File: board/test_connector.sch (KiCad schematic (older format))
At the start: 1 part, among them P1 test_connector

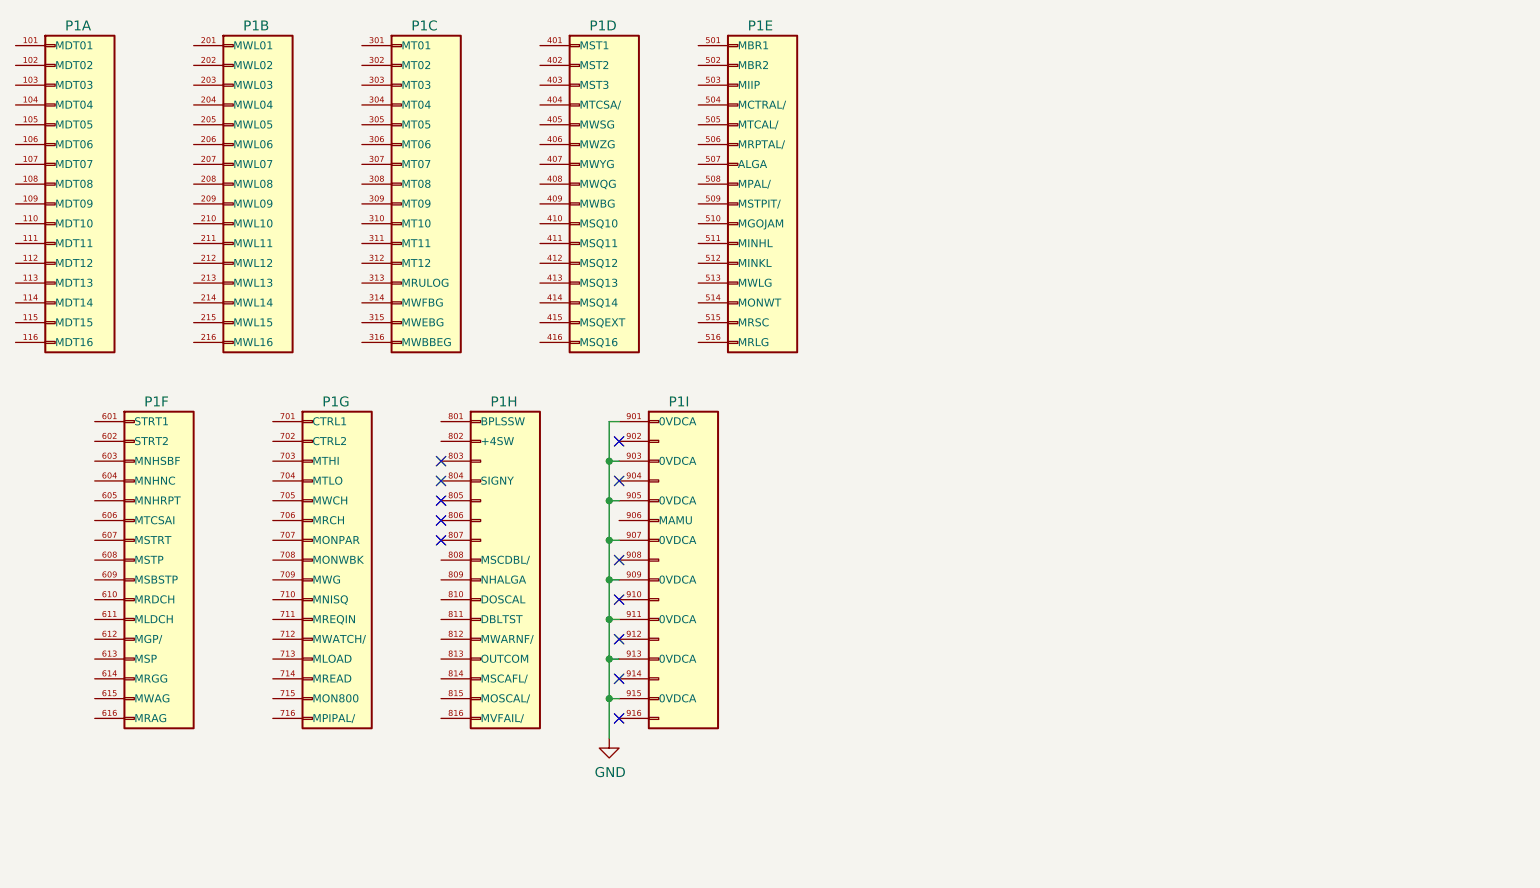
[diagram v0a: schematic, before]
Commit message: Board: initial schematic for the monitor interface board
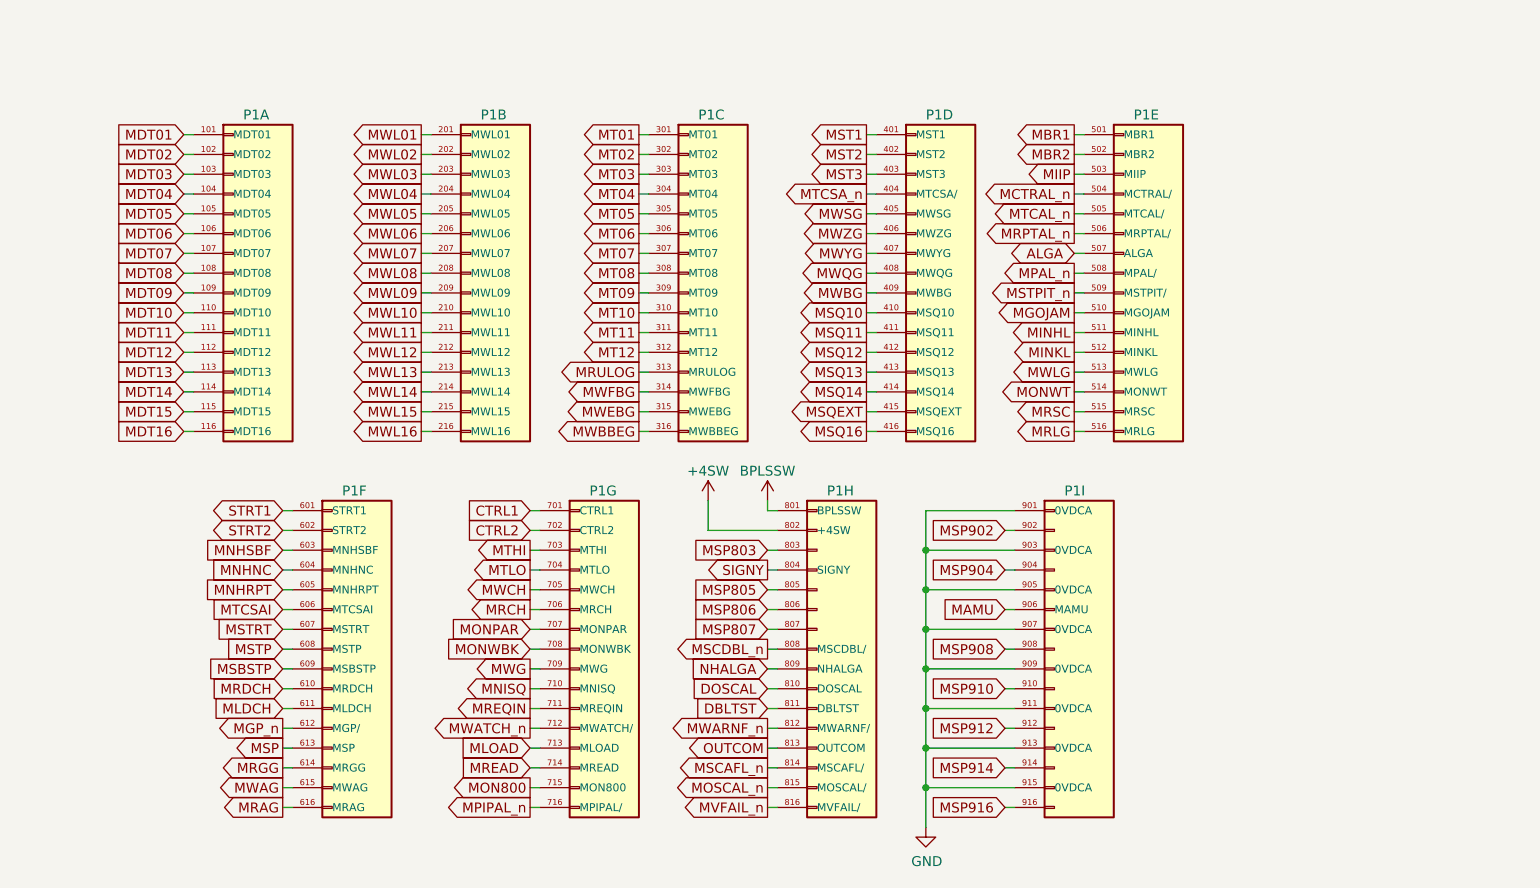
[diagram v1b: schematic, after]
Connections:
- net MDT01: now reaches P1.101 (MDT01)
- net MDT02: now reaches P1.102 (MDT02)
- net MDT03: now reaches P1.103 (MDT03)
- net MDT04: now reaches P1.104 (MDT04)
- net MDT05: now reaches P1.105 (MDT05)
- net MDT06: now reaches P1.106 (MDT06)
- net MDT07: now reaches P1.107 (MDT07)
- net MDT08: now reaches P1.108 (MDT08)
- net MDT09: now reaches P1.109 (MDT09)
- net MDT10: now reaches P1.110 (MDT10)
- net MDT11: now reaches P1.111 (MDT11)
- net MDT12: now reaches P1.112 (MDT12)
- net MDT13: now reaches P1.113 (MDT13)
- net MDT14: now reaches P1.114 (MDT14)
- net MDT15: now reaches P1.115 (MDT15)
- net MDT16: now reaches P1.116 (MDT16)
- net MWL01: now reaches P1.201 (MWL01)
- net MWL02: now reaches P1.202 (MWL02)
- net MWL03: now reaches P1.203 (MWL03)
- net MWL04: now reaches P1.204 (MWL04)
- net MWL05: now reaches P1.205 (MWL05)
- net MWL06: now reaches P1.206 (MWL06)
- net MWL07: now reaches P1.207 (MWL07)
- net MWL08: now reaches P1.208 (MWL08)
- net MWL09: now reaches P1.209 (MWL09)
- net MWL10: now reaches P1.210 (MWL10)
- net MWL11: now reaches P1.211 (MWL11)
- net MWL12: now reaches P1.212 (MWL12)
- net MWL13: now reaches P1.213 (MWL13)
- net MWL14: now reaches P1.214 (MWL14)
- net MWL15: now reaches P1.215 (MWL15)
- net MWL16: now reaches P1.216 (MWL16)
- net MT01: now reaches P1.301 (MT01)
- net MT02: now reaches P1.302 (MT02)
- net MT03: now reaches P1.303 (MT03)
- net MT04: now reaches P1.304 (MT04)
- net MT05: now reaches P1.305 (MT05)
- net MT06: now reaches P1.306 (MT06)
- net MT07: now reaches P1.307 (MT07)
- net MT08: now reaches P1.308 (MT08)
- net MT09: now reaches P1.309 (MT09)
- net MT10: now reaches P1.310 (MT10)
- net MT11: now reaches P1.311 (MT11)
- net MT12: now reaches P1.312 (MT12)
- net MRULOG: now reaches P1.313 (MRULOG)
- net MWFBG: now reaches P1.314 (MWFBG)
- net MWEBG: now reaches P1.315 (MWEBG)
- net MWBBEG: now reaches P1.316 (MWBBEG)
- net MST1: now reaches P1.401 (MST1)
- net MST2: now reaches P1.402 (MST2)
- net MST3: now reaches P1.403 (MST3)
- net MTCSA_n: now reaches P1.404 (MTCSA/)
- net MWSG: now reaches P1.405 (MWSG)
- net MWZG: now reaches P1.406 (MWZG)
- net MWYG: now reaches P1.407 (MWYG)
- net MWQG: now reaches P1.408 (MWQG)
- net MWBG: now reaches P1.409 (MWBG)
- net MSQ10: now reaches P1.410 (MSQ10)
- net MSQ11: now reaches P1.411 (MSQ11)
- net MSQ12: now reaches P1.412 (MSQ12)
- net MSQ13: now reaches P1.413 (MSQ13)
- net MSQ14: now reaches P1.414 (MSQ14)
- net MSQEXT: now reaches P1.415 (MSQEXT)
- net MSQ16: now reaches P1.416 (MSQ16)
- net MBR1: now reaches P1.501 (MBR1)
- net MBR2: now reaches P1.502 (MBR2)
- net MIIP: now reaches P1.503 (MIIP)
- net MCTRAL_n: now reaches P1.504 (MCTRAL/)
- net MTCAL_n: now reaches P1.505 (MTCAL/)
- net MRPTAL_n: now reaches P1.506 (MRPTAL/)
- net ALGA: now reaches P1.507 (ALGA)
- net MPAL_n: now reaches P1.508 (MPAL/)
- net MSTPIT_n: now reaches P1.509 (MSTPIT/)
- net MGOJAM: now reaches P1.510 (MGOJAM)
- net MINHL: now reaches P1.511 (MINHL)
- net MINKL: now reaches P1.512 (MINKL)
- net MWLG: now reaches P1.513 (MWLG)
- net MONWT: now reaches P1.514 (MONWT)
- net MRSC: now reaches P1.515 (MRSC)
- net MRLG: now reaches P1.516 (MRLG)
- net STRT1: now reaches P1.601 (STRT1)
- net STRT2: now reaches P1.602 (STRT2)
- net MNHSBF: now reaches P1.603 (MNHSBF)
- net MNHNC: now reaches P1.604 (MNHNC)
- net MNHRPT: now reaches P1.605 (MNHRPT)
- net MTCSAI: now reaches P1.606 (MTCSAI)
- net MSTRT: now reaches P1.607 (MSTRT)
- net MSTP: now reaches P1.608 (MSTP)
- net MSBSTP: now reaches P1.609 (MSBSTP)
- net MRDCH: now reaches P1.610 (MRDCH)
- net MLDCH: now reaches P1.611 (MLDCH)
- net MGP_n: now reaches P1.612 (MGP/)
- net MSP: now reaches P1.613 (MSP)
- net MRGG: now reaches P1.614 (MRGG)
- net MWAG: now reaches P1.615 (MWAG)
- net MRAG: now reaches P1.616 (MRAG)
- net CTRL1: now reaches P1.701 (CTRL1)
- net CTRL2: now reaches P1.702 (CTRL2)
- net MTHI: now reaches P1.703 (MTHI)
- net MTLO: now reaches P1.704 (MTLO)
- net MWCH: now reaches P1.705 (MWCH)
- net MRCH: now reaches P1.706 (MRCH)
- net MONPAR: now reaches P1.707 (MONPAR)
- net MONWBK: now reaches P1.708 (MONWBK)
- net MWG: now reaches P1.709 (MWG)
- net MNISQ: now reaches P1.710 (MNISQ)
- net MREQIN: now reaches P1.711 (MREQIN)
- net MWATCH_n: now reaches P1.712 (MWATCH/)
- net MLOAD: now reaches P1.713 (MLOAD)
- net MREAD: now reaches P1.714 (MREAD)
- net MON800: now reaches P1.715 (MON800)
- net MPIPAL_n: now reaches P1.716 (MPIPAL/)
- net BPLSSW: now reaches P1.801 (BPLSSW)
- net +4SW: now reaches P1.802 (+4SW)
- net MSP803: now reaches P1.803
- net SIGNY: now reaches P1.804 (SIGNY)
- net MSP805: now reaches P1.805
- net MSP806: now reaches P1.806
- net MSP807: now reaches P1.807
- net MSCDBL_n: now reaches P1.808 (MSCDBL/)
- net NHALGA: now reaches P1.809 (NHALGA)
- net DOSCAL: now reaches P1.810 (DOSCAL)
- net DBLTST: now reaches P1.811 (DBLTST)
- net MWARNF_n: now reaches P1.812 (MWARNF/)
- net OUTCOM: now reaches P1.813 (OUTCOM)
- net MSCAFL_n: now reaches P1.814 (MSCAFL/)
- net MOSCAL_n: now reaches P1.815 (MOSCAL/)
- net MVFAIL_n: now reaches P1.816 (MVFAIL/)
- net MSP902: now reaches P1.902
- net MSP904: now reaches P1.904
- net MAMU: now reaches P1.906 (MAMU)
- net MSP908: now reaches P1.908
- net MSP910: now reaches P1.910
- net MSP912: now reaches P1.912
- net MSP914: now reaches P1.914
- net MSP916: now reaches P1.916
- no-connect marks 12 -> 0
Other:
- moved on the sheet: P1A, P1B, P1C, P1D, P1E, P1F, P1G, P1H, P1I

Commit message: Board: minor schematic tweaks, footprint creation, and initial subcircuit layout
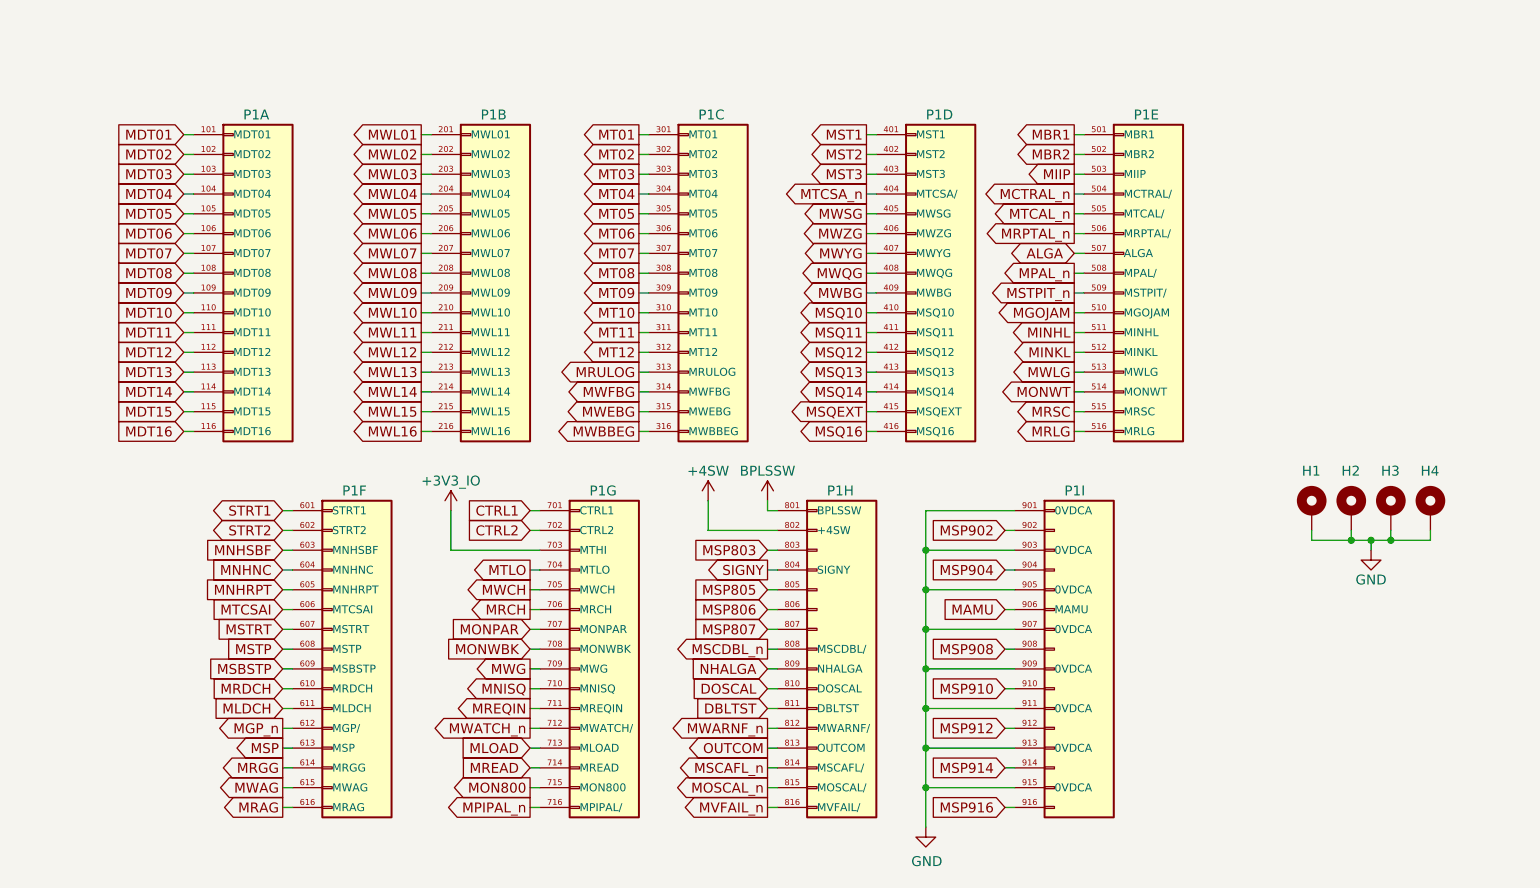
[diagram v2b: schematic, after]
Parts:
- added H1, H2, H3, H4: MountingHole_Pad, agc_monitor:MountingHole_1004579, symbol Mechanical:MountingHole_Pad
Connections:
- net GND: now also H1.1, H2.1, H3.1, H4.1
- net MTHI renamed +3V3_IO
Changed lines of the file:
@@
 U 1 1 5C348453
 P 3500 2650
+AR Path="/5C348453" Ref="P1"  Part="1"
+AR Path="/5C3483A0/5C348453" Ref="P1"  Part="1"
 F 0 "P1" H 3600 3450 50  0000 L CNN
 F 1 "test_connector" H 3879 2555 50  0001 L CNN
@@
 U 2 1 5C34852D
 P 4700 2650
+AR Path="/5C34852D" Ref="P1"  Part="2"
+AR Path="/5C3483A0/5C34852D" Ref="P1"  Part="2"
 F 0 "P1" H 4800 3450 50  0000 L CNN
 F 1 "test_connector" H 5079 2555 50  0001 L CNN
@@
 U 3 1 5C348601
 P 5800 2650
+AR Path="/5C348601" Ref="P1"  Part="3"
+AR Path="/5C3483A0/5C348601" Ref="P1"  Part="3"
 F 0 "P1" H 5900 3450 50  0000 L CNN
 F 1 "test_connector" H 6179 2555 50  0001 L CNN
@@
 U 4 1 5C348607
 P 6950 2650
+AR Path="/5C348607" Ref="P1"  Part="4"
+AR Path="/5C3483A0/5C348607" Ref="P1"  Part="4"
 F 0 "P1" H 7050 3450 50  0000 L CNN
 F 1 "test_connector" H 7329 2555 50  0001 L CNN
@@
 U 5 1 5C3486F3
 P 8000 2650
+AR Path="/5C3486F3" Ref="P1"  Part="5"
+AR Path="/5C3483A0/5C3486F3" Ref="P1"  Part="5"
 F 0 "P1" H 8100 3450 50  0000 L CNN
 F 1 "test_connector" H 8379 2555 50  0001 L CNN
@@
 U 6 1 5C3487FE
 P 4000 4550
+AR Path="/5C3487FE" Ref="P1"  Part="6"
+AR Path="/5C3483A0/5C3487FE" Ref="P1"  Part="6"
 F 0 "P1" H 4100 5350 50  0000 L CNN
 F 1 "test_connector" H 4379 4455 50  0001 L CNN
@@
 U 7 1 5C348804
 P 5250 4550
+AR Path="/5C348804" Ref="P1"  Part="7"
+AR Path="/5C3483A0/5C348804" Ref="P1"  Part="7"
 F 0 "P1" H 5350 5350 50  0000 L CNN
 F 1 "test_connector" H 5629 4455 50  0001 L CNN
@@
 U 9 1 5C348810
 P 7650 4550
+AR Path="/5C348810" Ref="P1"  Part="9"
+AR Path="/5C3483A0/5C348810" Ref="P1"  Part="9"
 F 0 "P1" H 7750 5350 50  0000 L CNN
 F 1 "test_connector" H 8029 4455 50  0001 L CNN
@@
 Connection ~ 7050 4050
 Wire Wire Line
-	7050 4050 7050 4250
-Wire Wire Line
-	7500 4250 7050 4250
-Connection ~ 7050 4250
-Wire Wire Line
-	7050 4250 7050 4450
-Wire Wire Line
 	7500 4450 7050 4450
 Connection ~ 7050 4450
@@
 	7500 4650 7050 4650
 Connection ~ 7050 4650
-Wire Wire Line
-	7050 4650 7050 4850
-Wire Wire Line
-	7500 4850 7050 4850
-Connection ~ 7050 4850
-Wire Wire Line
-	7050 4850 7050 5050
 Wire Wire Line
 	7500 5050 7050 5050
@@
 Wire Wire Line
 	5050 3950 5100 3950
-Text GLabel 5050 4050 0    50   Output ~ 0
-MTHI
-Wire Wire Line
-	5100 4050 5050 4050
 Text GLabel 5050 4150 0    50   Output ~ 0
 MTLO
@@
 U 8 1 5C34880A
 P 6450 4550
+AR Path="/5C34880A" Ref="P1"  Part="8"
+AR Path="/5C3483A0/5C34880A" Ref="P1"  Part="8"
 F 0 "P1" H 6550 5350 50  0000 L CNN
 F 1 "test_connector" H 6829 4455 50  0001 L CNN
@@
 Wire Wire Line
 	5950 3950 6300 3950
+Wire Wire Line
+	7050 4650 7050 4850
+Wire Wire Line
+	7050 4850 7500 4850
+Connection ~ 7050 4850
+Wire Wire Line
+	7050 4850 7050 5050
+Wire Wire Line
+	7050 4050 7050 4250
+Wire Wire Line
+	7500 4250 7050 4250
+Connection ~ 7050 4250
+Wire Wire Line
+	7050 4250 7050 4450
+$Comp
+L Mechanical:MountingHole_Pad H1
+U 1 1 5C7A2299
+P 9000 3850
+F 0 "H1" H 8950 4050 50  0000 L CNN
+F 1 "MountingHole_Pad" H 9100 3810 50  0001 L CNN
+F 2 "agc_monitor:MountingHole_1004579" H 9000 3850 50  0001 C CNN
+F 3 "~" H 9000 3850 50  0001 C CNN
+	1    9000 3850
+	1    0    0    -1
+$EndComp
+$Comp
+L power:GND #PWR0160
+U 1 1 5C7A2406
+P 9300 4050
+F 0 "#PWR0160" H 9300 3800 50  0001 C CNN
+F 1 "GND" H 9300 3900 50  0000 C CNN
+F 2 "" H 9300 4050 50  0001 C CNN
+F 3 "" H 9300 4050 50  0001 C CNN
+	1    9300 4050
+	1    0    0    -1
+$EndComp
+$Comp
+L Mechanical:MountingHole_Pad H2
+U 1 1 5C7A332F
+P 9200 3850
+F 0 "H2" H 9150 4050 50  0000 L CNN
+F 1 "MountingHole_Pad" H 9300 3810 50  0001 L CNN
+F 2 "agc_monitor:MountingHole_1004579" H 9200 3850 50  0001 C CNN
+F 3 "~" H 9200 3850 50  0001 C CNN
+	1    9200 3850
+	1    0    0    -1
+$EndComp
+$Comp
+L Mechanical:MountingHole_Pad H3
+U 1 1 5C7AD28E
+P 9400 3850
+F 0 "H3" H 9350 4050 50  0000 L CNN
+F 1 "MountingHole_Pad" H 9500 3810 50  0001 L CNN
+F 2 "agc_monitor:MountingHole_1004579" H 9400 3850 50  0001 C CNN
+F 3 "~" H 9400 3850 50  0001 C CNN
+	1    9400 3850
+	1    0    0    -1
+$EndComp
+$Comp
+L Mechanical:MountingHole_Pad H4
+U 1 1 5C7B71F2
+P 9600 3850
+F 0 "H4" H 9550 4050 50  0000 L CNN
+F 1 "MountingHole_Pad" H 9700 3810 50  0001 L CNN
+F 2 "agc_monitor:MountingHole_1004579" H 9600 3850 50  0001 C CNN
+F 3 "~" H 9600 3850 50  0001 C CNN
+	1    9600 3850
+	1    0    0    -1
+$EndComp
+Wire Wire Line
+	9000 3950 9000 4000
+Wire Wire Line
+	9000 4000 9200 4000
+Wire Wire Line
+	9300 4000 9300 4050
+Wire Wire Line
+	9300 4000 9400 4000
+Wire Wire Line
+	9600 4000 9600 3950
+Connection ~ 9300 4000
+Wire Wire Line
+	9400 3950 9400 4000
+Connection ~ 9400 4000
+Wire Wire Line
+	9400 4000 9600 4000
+Wire Wire Line
+	9200 3950 9200 4000
+Connection ~ 9200 4000
+Wire Wire Line
+	9200 4000 9300 4000
+$Comp
+L agc_monitor:+3V3_IO #PWR0135
+U 1 1 5D82059E
+P 4650 3850
+F 0 "#PWR0135" H 4650 3700 50  0001 C CNN
+F 1 "+3V3_IO" H 4650 4000 50  0000 C CNN
+F 2 "" H 4650 3850 50  0001 C CNN
+F 3 "" H 4650 3850 50  0001 C CNN
+	1    4650 3850
+	1    0    0    -1
+$EndComp
+Wire Wire Line
+	4650 3850 4650 4050
+Wire Wire Line
+	4650 4050 5100 4050
 $EndSCHEMATC
